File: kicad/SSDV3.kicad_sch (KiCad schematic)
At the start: 8 parts, among them J7 SM02B-GHS-TB(LF)(SN), J8 SM03B-GHS-TB(LF)(SN)

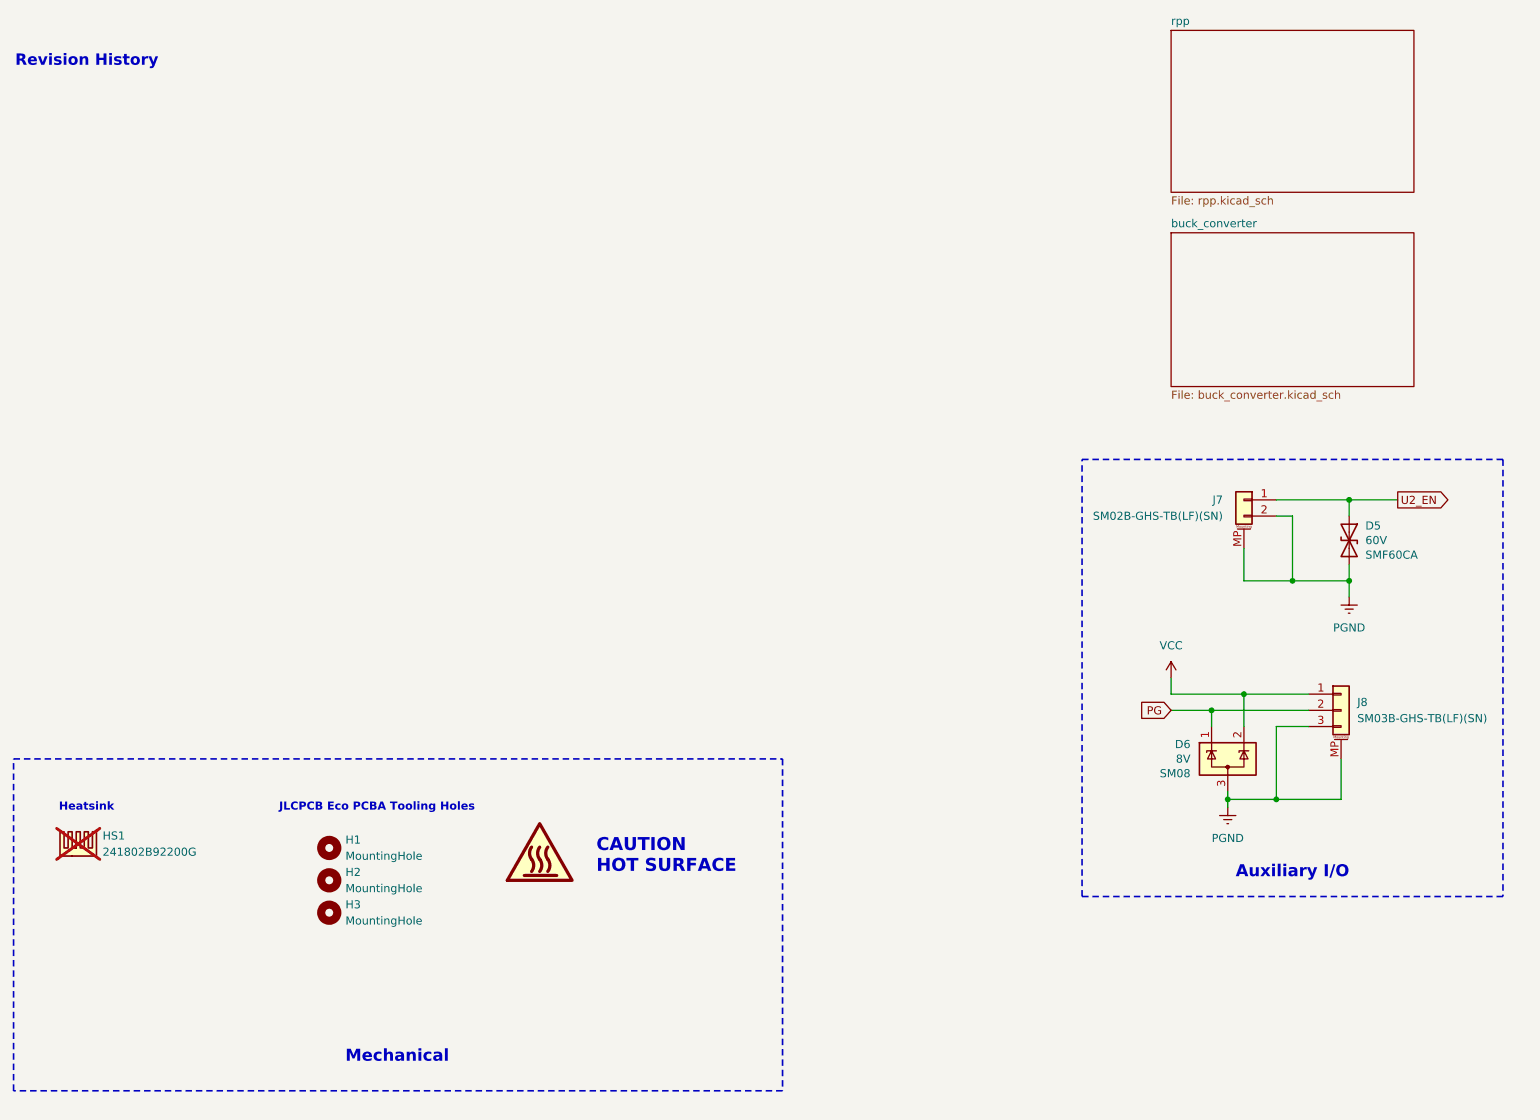
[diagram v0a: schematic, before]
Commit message: Added UBCO trademark notice, prepared for production
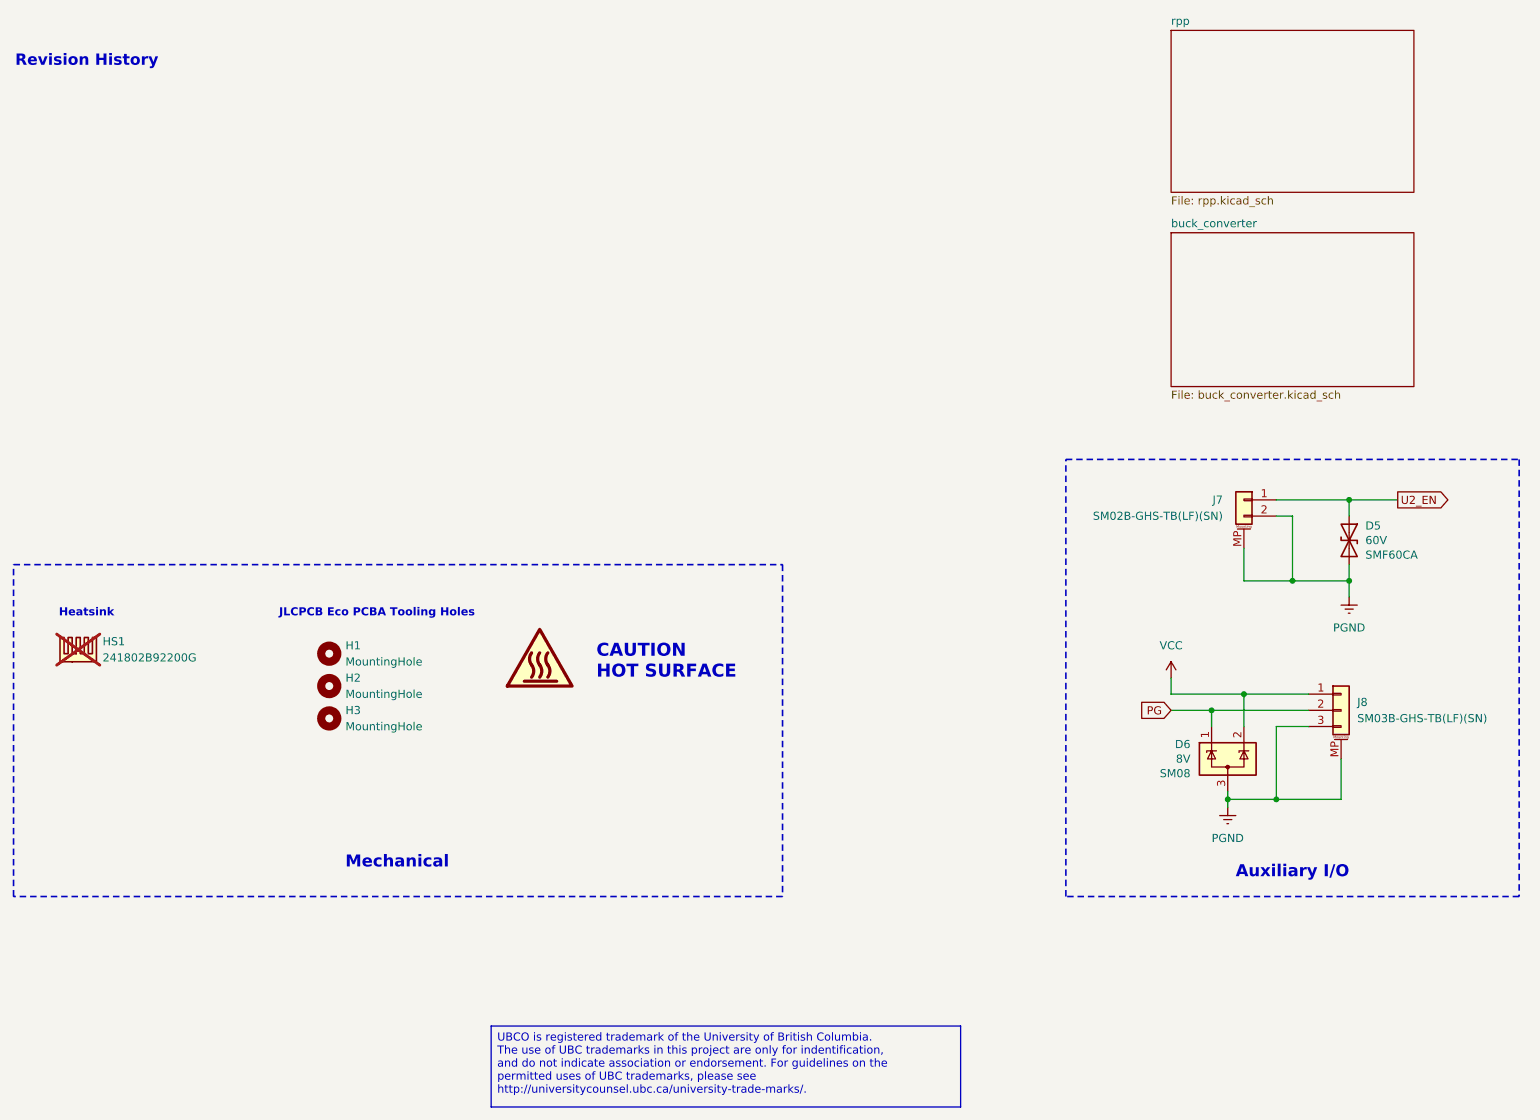
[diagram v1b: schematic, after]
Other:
- company: Author: Julian Joaquin -> UBCO Aerospace
- moved on the sheet: H1, H2, H3, HS1

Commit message: Component optimizations
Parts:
- J7: now left out of the parts list
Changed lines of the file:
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@@
 		(unit 1)
 		(exclude_from_sim no)
-		(in_bom yes)
+		(in_bom no)
 		(on_board yes)
 		(dnp no)
